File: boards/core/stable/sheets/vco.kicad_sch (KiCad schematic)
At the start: 54 parts, among them Q201 2N3906, Q202 BC847BS, Q203 MMBFJ111, Q211 J111, Q301 MMBT5551, U201 TL072, U202 TL072, U203 LM311

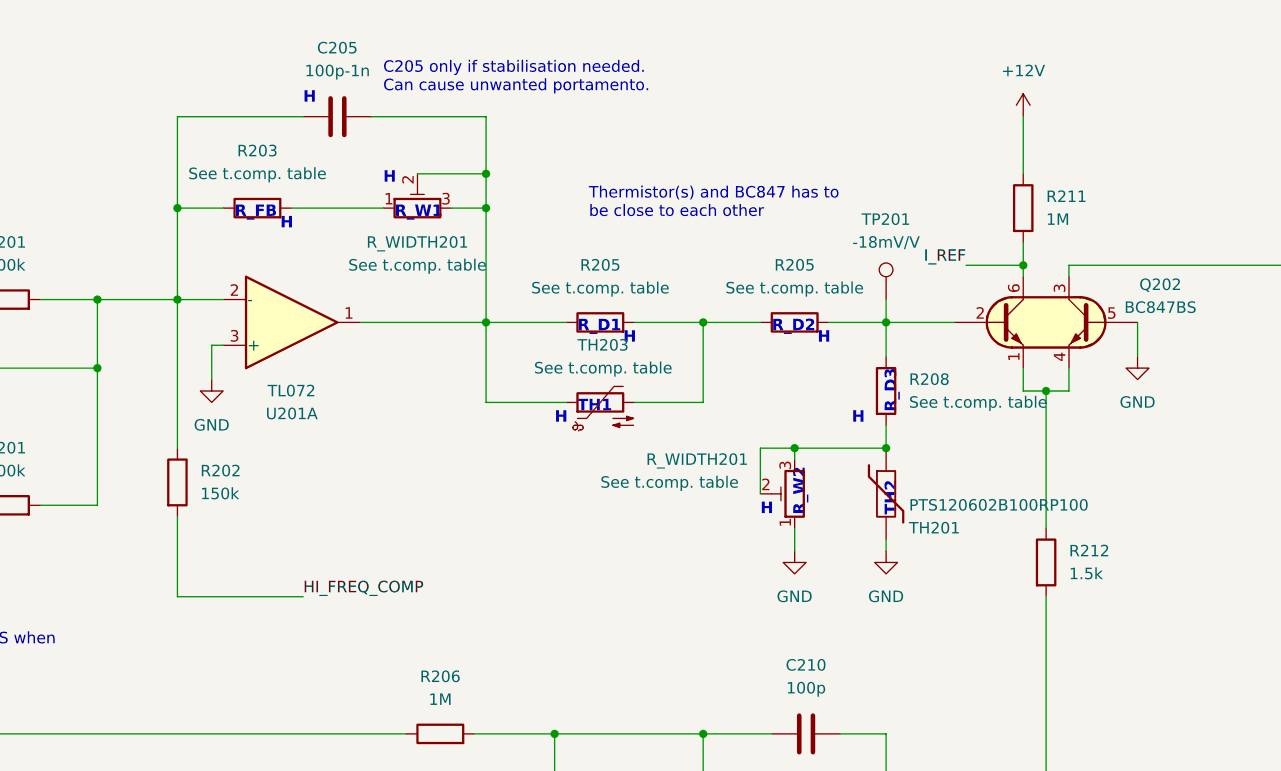
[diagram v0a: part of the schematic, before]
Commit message: Streamline 'Stable' Core board
https://github.com/shmoergh/hog/issues/7

- Remove 12V terminal input
- Reposition Eurorack power connector to right so it makes space for tuning
- Remove all unnecessary thermal compensation pseudo components
- Reposition tuning trimmers
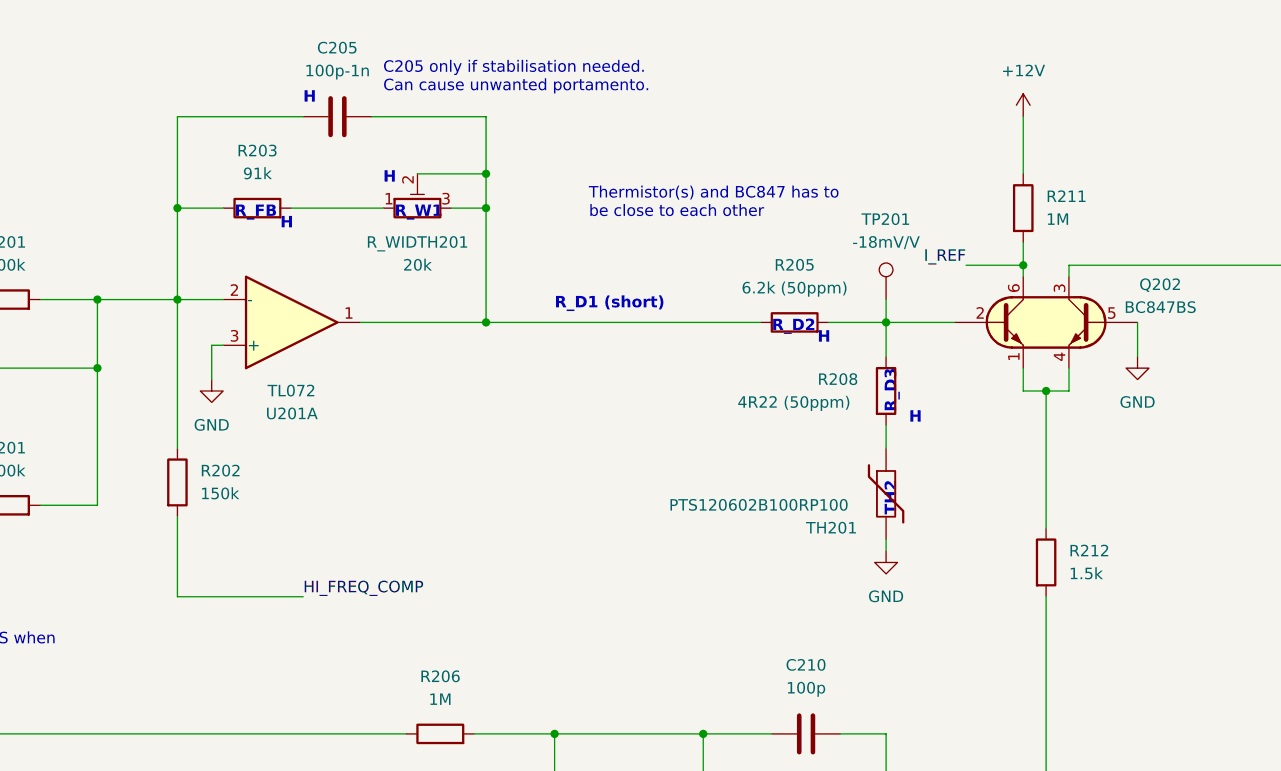
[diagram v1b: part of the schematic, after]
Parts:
- removed R205: See t.comp. table, Shmoergh_Custom_Footprints:R_Axial_DIN0207_L6.3mm_D2.5mm_P7.62mm_Horizontal, symbol Device:R
- removed R_WIDTH201: See t.comp. table, Potentiometer_THT:Potentiometer_Bourns_3006P_Horizontal, symbol Device:R_Potentiometer_Trim
- removed TH203: See t.comp. table, Package_TO_SOT_THT:TO-92-2, symbol Device:Thermistor_NTC
- Q202: footprint Package_TO_SOT_SMD:SOT-363_SC-70-6 -> Package_TO_SOT_SMD:SOT-363_SC-70-6_Handsoldering
- R203: value See t.comp. table -> 91k
- R205: value See t.comp. table -> 6.2k (50ppm)
- R208: value See t.comp. table -> 4R22 (50ppm)
- R_WIDTH201: value See t.comp. table -> 20k
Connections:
- net at R205.1: now also C205.2, R_WIDTH201.2, R_WIDTH201.3, U201.1
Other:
- note added: "R_D1 (short)"
- note removed: "R_D1"
- note removed: "R_W2"
- note removed: "TH1"

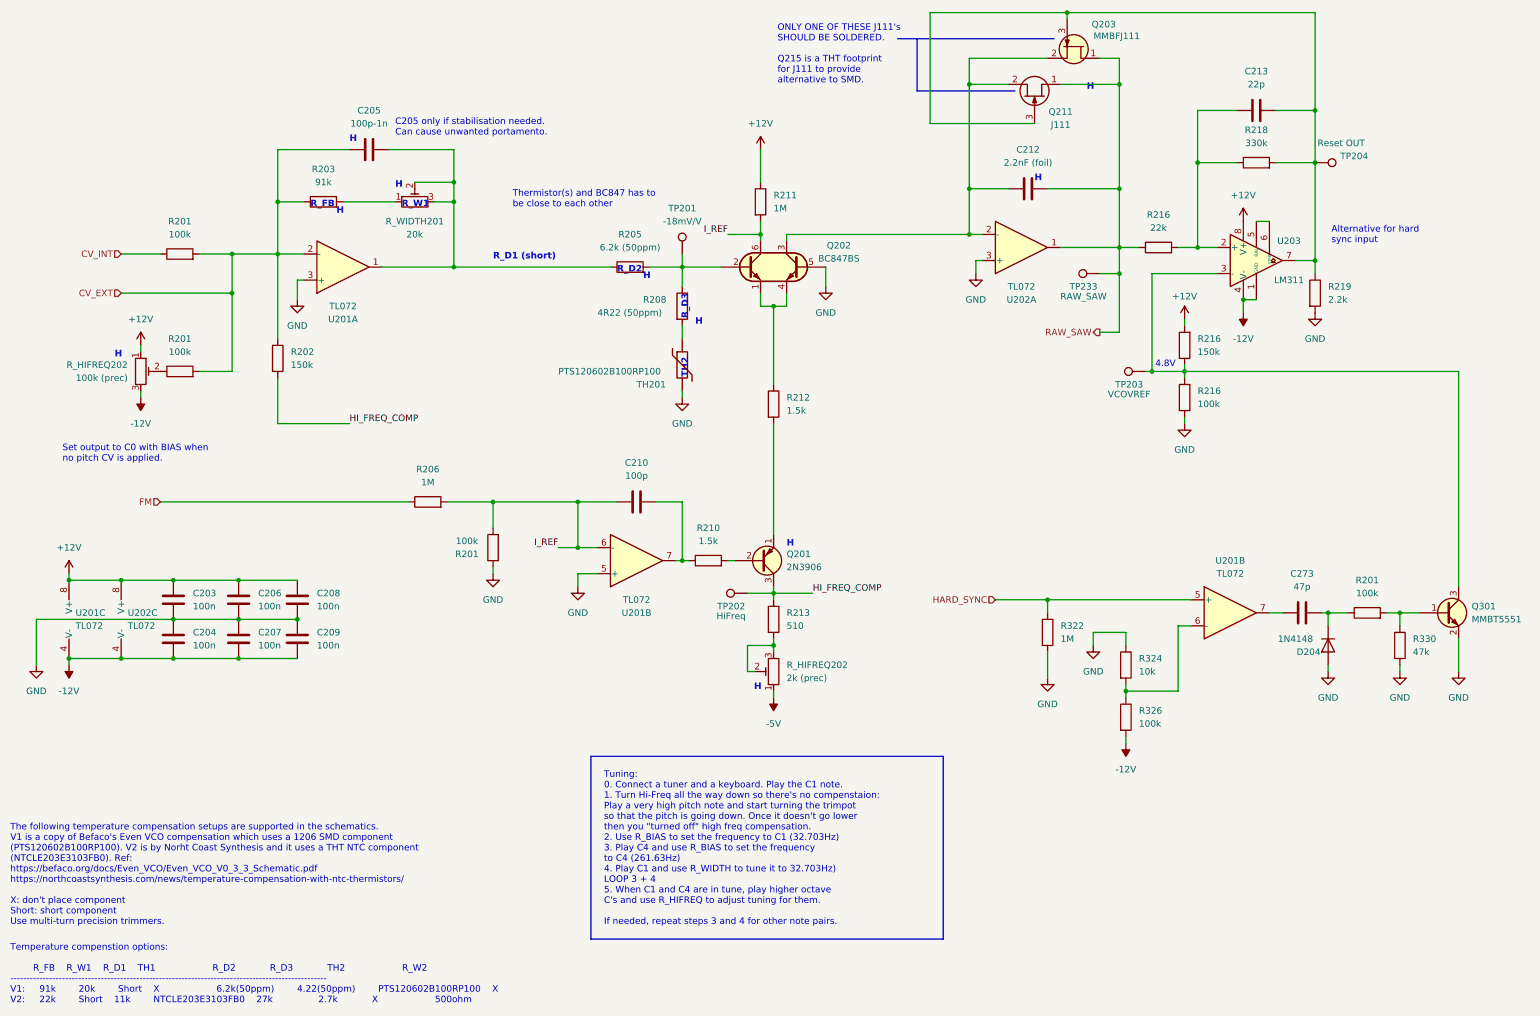
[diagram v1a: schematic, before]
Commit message: Updated and checked Core board BOM
ref https://github.com/shmoergh/hog/issues/19
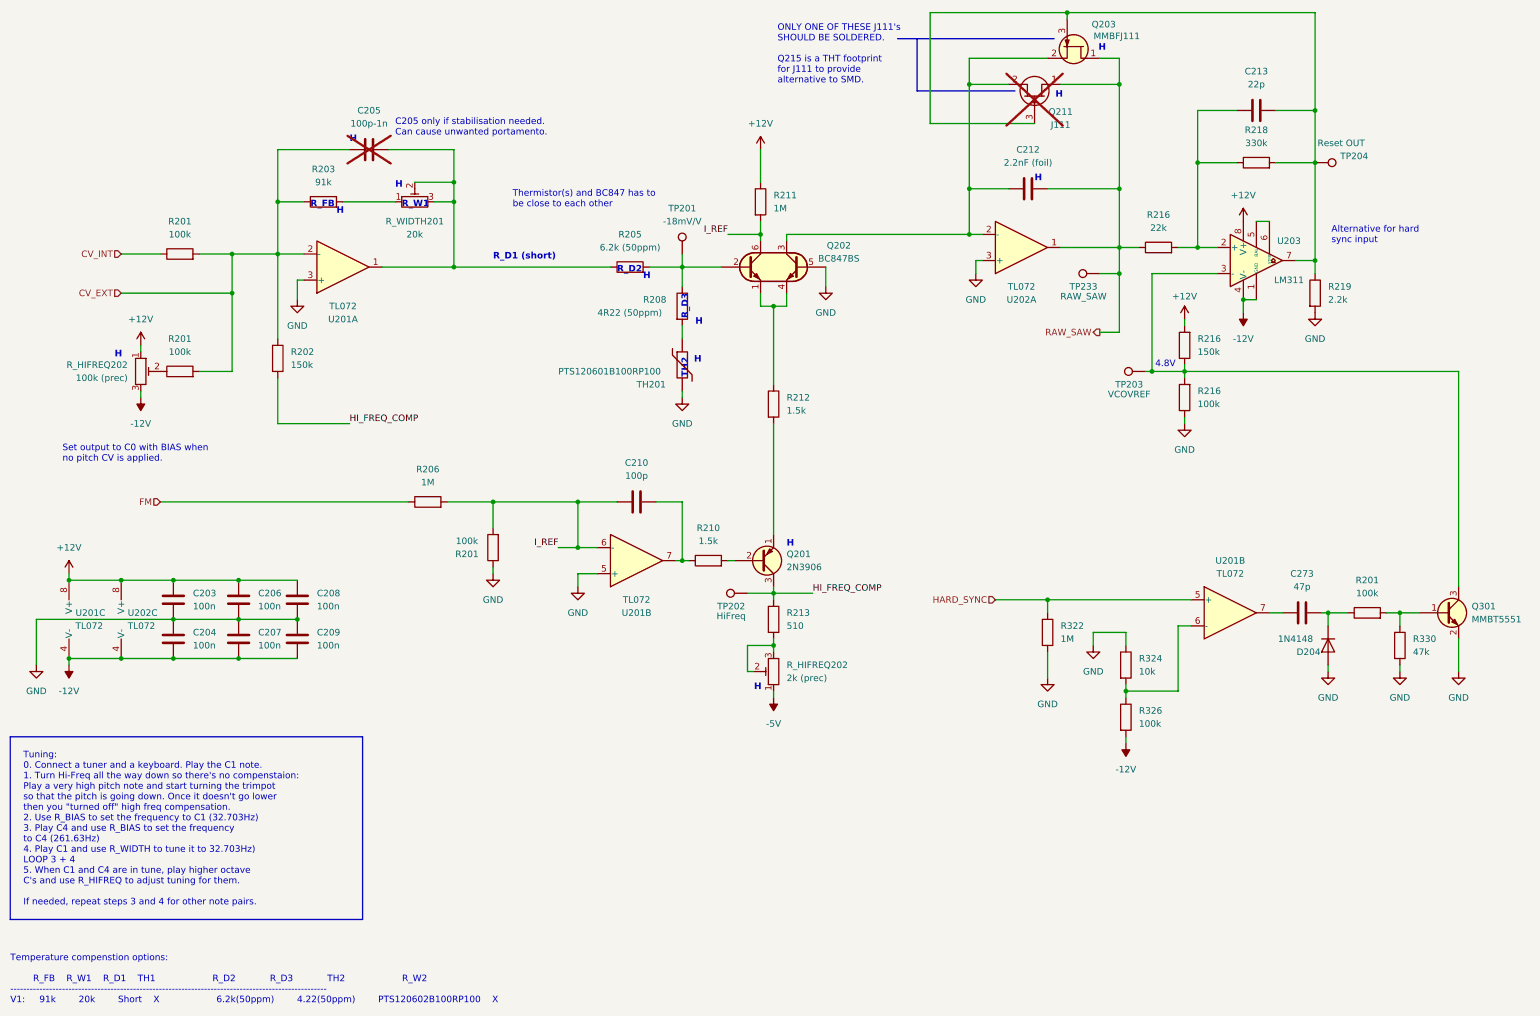
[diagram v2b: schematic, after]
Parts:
- C203, C204, C206, C207, C208, C209, C210, C213, C273, D204, Q301, R201, R202, R206, R210, R211, R212, R213, R216, R218, R219, R322, R324, R326, R330, U201, U202, U203: Vendor (none) -> JLCPCB
- C205: now not fitted
- C212: Part No. (none) -> 80-R82EC1220AA50J; Part URL (none) -> https://mou.sr/3y3T8LM; Vendor (none) -> Mouser
- Q201: Part No. (none) -> 512-2N3906BU; Part URL (none) -> https://mou.sr/3ZrOXn8; Vendor (none) -> Mouser; now in the parts list
- Q202: LCSC C699265 -> C5380687; Vendor (none) -> JLCPCB
- Q203: LCSC C274688 -> (none); Part No. (none) -> 512-MMBFJ111; Part URL (none) -> https://mou.sr/3Us0WP4; Vendor (none) -> Mouser; now in the parts list
- Q211: Mouser 512-J111 -> (none); Part No. (none) -> 512-J111; Part URL (none) -> https://mou.sr/4f5W0HS; Vendor (none) -> Mouser; now not fitted
- R203: Hestore https://www.hestore.hu/prod_10020570.html -> (none); Part No. (none) -> 603-MFR50SFTE52-91K; Part URL (none) -> https://mou.sr/3Vwa9XS; Vendor (none) -> Mouser; now in the parts list
- R205: Part No. (none) -> 603-MFR50SFTE52-6K2; Part URL (none) -> https://mou.sr/3OL65PP; Vendor (none) -> Mouser; now in the parts list
- R208: Mouser https://hu.mouser.com/ProductDetail/YAGEO/MFR50SFTE52-4R22?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 -> (none); Part No. (none) -> 603-MFR50SFTE52-4R22; Part URL (none) -> https://mou.sr/49tYeQ0; Vendor (none) -> Mouser; now in the parts list
- R_HIFREQ202: Part No. (none) -> 652-3006P-1-202-LF; Part URL (none) -> https://mou.sr/3ZK9AMt; Vendor (none) -> Mouser
- R_HIFREQ202: Arwill https://arwill.hu/termekek/passziv-alkatreszek/trimmer-potm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 -> (none); Part No. (none) -> 652-3006P-1-104-LF; Part URL (none) -> https://mou.sr/4ff5W1E; Vendor (none) -> Mouser
- R_WIDTH201: Part No. (none) -> 652-3006P-7-203-LF; Part URL (none) -> https://mou.sr/41re1x3; Vendor (none) -> Mouser; now in the parts list
- TH201: value PTS120602B100RP100 -> PTS120601B100RP100; Mouser https://hu.mouser.com/ProductDetail/594-PTS120601B100RP -> (none); Part No. (none) -> 594-PTS120601B100RP; Part URL (none) -> https://mou.sr/4g7SsGi; Vendor (none) -> Mouser; now in the parts list
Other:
- note added: "Temperature compenstion options: R_FB R_W1 R_D1 TH1 R_D2 R_D3 TH2 R_W2 -------------------------------------------------------------------------------------------------- V1: 91k 20k Short X 6.2k(50ppm) 4.22(50ppm) PTS120602B100RP100 X"
- note removed: "Temperature compenstion options: R_FB R_W1 R_D1 TH1 R_D2 R_D3 TH2 R_W2 -------------------------------------------------------------------------------------------------- V1: 91k 20k Short X 6.2k(50ppm) 4.22(50ppm) PTS120602B100RP100 X V2: 22k Short 11k NTCLE203E3103FB0 27k 2.7k X 500ohm"
- note removed: "The following temperature compensation setups are supported in the schematics. V1 is a copy of Befaco's Even VCO compensation which uses a 1206 SMD component (PTS120602B100RP100). V2 is by Norht Coast Synthesis and it uses a THT NTC component (NTCLE203E3103FB0). Ref: https://befaco.org/docs/Even_VCO/Even_VCO_V0_3_3_Schematic.pdf https://northcoastsynthesis.com/news/temperature-compensation-with-n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"
